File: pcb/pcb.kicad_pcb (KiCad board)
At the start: 2 copper layers, 35 x 30 mm, 43 parts, among them IC1 TC78H660FTG,EL, J1 Screw_Terminal_01x02, J2 Conn_01x06_Male, J3 Screw_Terminal_01x02, J4 Screw_Terminal_01x02, Q1 Q_PMOS_GSD, U1 ME431

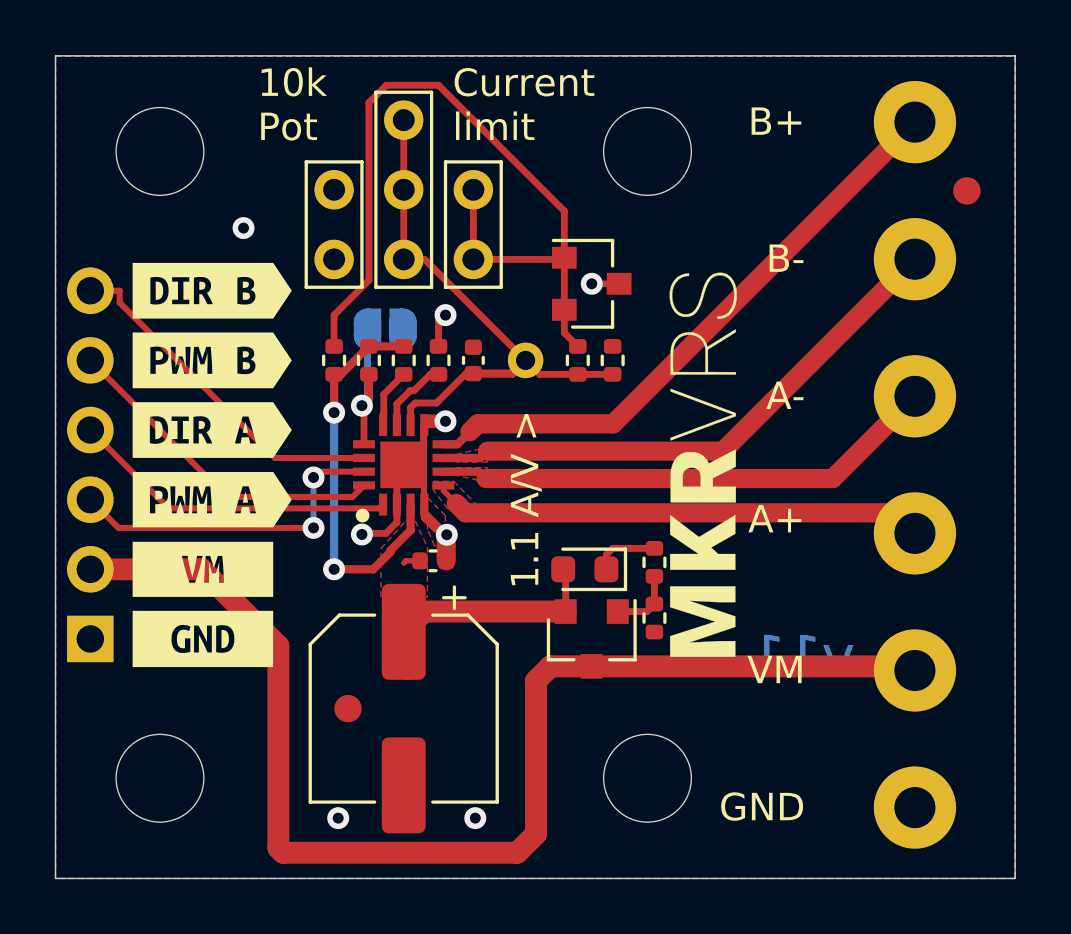
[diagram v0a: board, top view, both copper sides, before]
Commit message: v20 update with voltage regulator
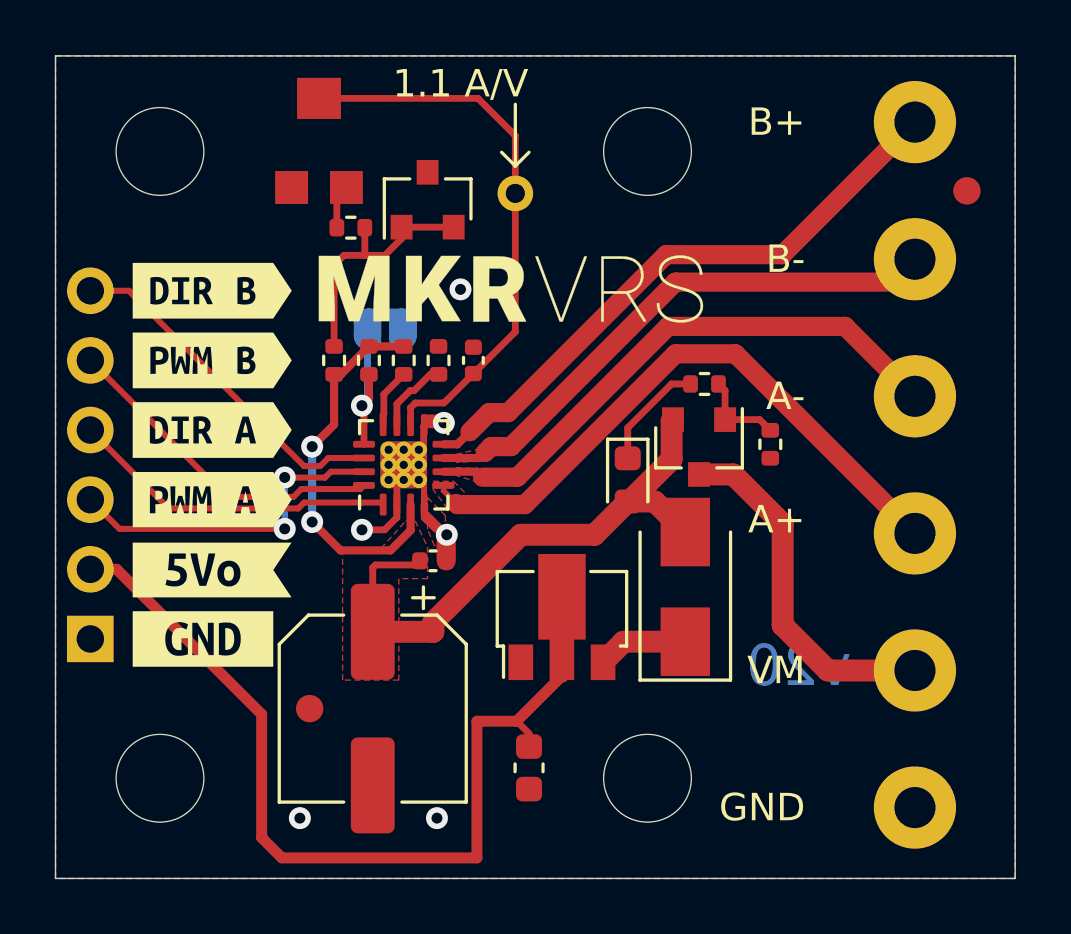
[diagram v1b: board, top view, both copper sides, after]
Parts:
- removed R6: 14k, Resistor_SMD:R_0402_1005Metric
- removed kibuzzard-611F05D8 (x2), kibuzzard-611F05E5, kibuzzard-611F1057: G***, label
- added C4: 10uF, Capacitor_SMD:C_0603_1608Metric, F.Cu at (150.1, 115.8)
- added D2: D_Schottky, Diode_SMD:D_SMA, F.Cu at (155.8, 109.2)
- added U2: AMS1117-5.0 SOT-89, Package_TO_SOT_SMD:SOT-89-3, F.Cu at (151.3, 110.3)
- added kibuzzard-62F06A1B: G***, kibuzzard-62F06A1B, F.Cu at (138.2, 111.1)
- added kibuzzard-62F06A1B: G***, kibuzzard-62F06A1B, B.Cu at (138.2, 111.1)
- added kibuzzard-62F08A45: G***, kibuzzard-62F08A45, B.Cu at (138.6, 108.6)
- added kibuzzard-62F08A4D: G***, kibuzzard-62F08A4D, F.Cu at (138.6, 108.6)
- IC1: footprint lib:QFN50P300X300X90-17N -> Package_DFN_QFN:QFN-16-1EP_3x3mm_P0.5mm_EP1.7x1.7mm_ThermalVias
- R5: value 4k7 -> 20k
- RV1: value R_POT -> 50k; footprint Potentiometer_THT:Potentiometer_Bourns_3296W_Vertical -> lib:smdPot
- moved R5 9.59 mm to (143.6, 96.1), turned to 180 degrees
- moved G*** 9.50 mm to (149.5, 98.4), turned to 0 degrees
- moved Q1 8.02 mm to (156.3, 104.1)
- moved R8 7.62 mm to (158.9, 104.0)
- moved RV1 7.16 mm to (142.5, 92.9)
- moved R7 6.76 mm to (156.5, 101.8), turned to 0 degrees
- moved U1 6.73 mm to (146.4, 95.1), turned to 90 degrees
- moved TP1 6.10 mm to (149.6, 94.9)
- moved D1 3.62 mm to (153.7, 105.3), turned to -90 degrees
- moved FID2 1.40 mm to (142.1, 113.7)
- moved C2 1.13 mm to (144.4, 113.7)
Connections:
- J2 pad 2: VDC -> Net-(C4-Pad1)
- R5 pad 2: Net-(C3-Pad1) -> Net-(R5-Pad2)
- RV1 pad 1: Net-(R2-Pad2) -> GND
- RV1 pad 3: GND -> Net-(R5-Pad2)
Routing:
- net VDC: track 44.8 -> 13.0 mm
- net Net-(C4-Pad1): track 0.00 -> 31.6 mm
- net Net-(R2-Pad2): track 29.7 -> 9.16 mm
- net VCC: track 23.0 -> 36.0 mm
- net Net-(IC1-Pad5): track 18.2 -> 22.8 mm
- net Net-(D2-Pad1): track 0.00 -> 3.31 mm
- net GND: track 16.1 -> 13.5 mm, vias 8 -> 6
- net Net-(IC1-Pad6): track 18.5 -> 20.5 mm
- net Net-(D1-Pad1): track 2.38 -> 4.07 mm
- net Net-(R5-Pad2): track 0.00 -> 1.61 mm
- net Net-(Q1-Pad1): track 2.46 -> 3.21 mm
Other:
- board text added: "1.1 A/V"
- board text added: "v20"
- board text removed: "1.1 A/V >"
- board text removed: "10k Pot"
- board text removed: "4x 3.2mm hole"
- board text removed: "Current limit"
- board text removed: "v11"
